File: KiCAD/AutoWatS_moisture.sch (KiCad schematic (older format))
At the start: 20 parts, among them J1 Conn_02x03_Odd_Even, J2 Conn_01x04, U1 ATtiny441-SSU, Y1 YSX321SL

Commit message: Fix Xtal footprint ref
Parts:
- Y1: footprint YSX321SL -> JLCPCB:YSX321SL
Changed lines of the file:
@@
 F 0 "Y1" V 6554 3378 50  0000 L CNN
 F 1 "YSX321SL" V 6645 3378 50  0000 L CNN
-F 2 "YSX321SL" H 7250 3350 50  0001 L CNN
+F 2 "JLCPCB:YSX321SL" H 7250 3350 50  0001 L CNN
 F 3 "https://datasheet.lcsc.com/szlcsc/YSX321SL-30MHZ-10PF-8PPM_C70576.pdf" H 7250 3250 50  0001 L CNN
 F 4 "Crystal" H 7250 3150 50  0001 L CNN "Description"

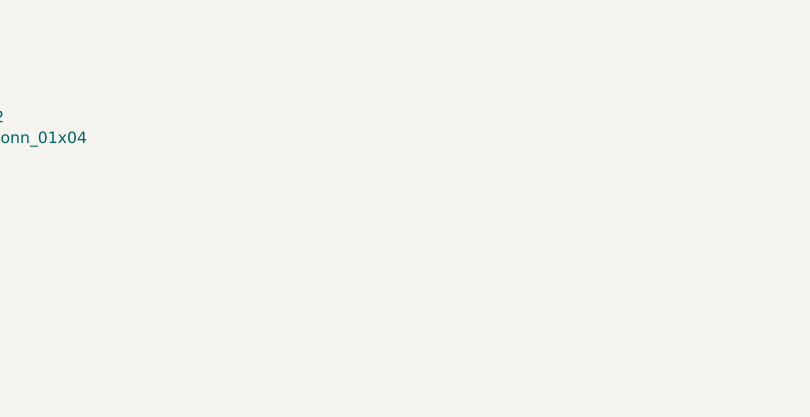
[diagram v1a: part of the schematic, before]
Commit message: Added debug port, silk info and changed the layout a bit
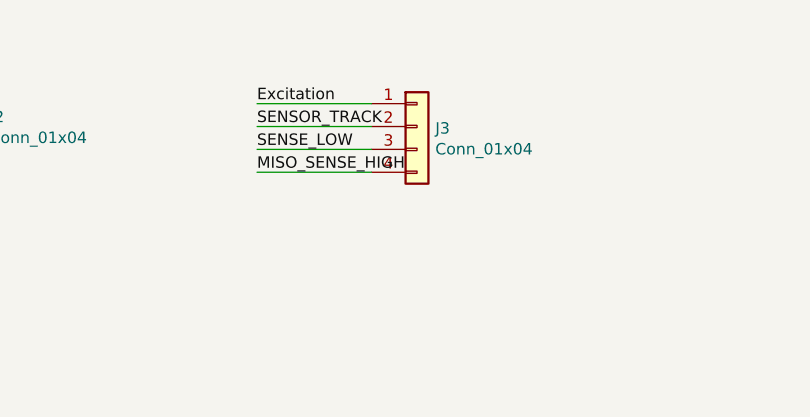
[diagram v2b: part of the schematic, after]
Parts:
- added J3: Conn_01x04, Connector_PinHeader_2.54mm:PinHeader_1x04_P2.54mm_Vertical, symbol Connector_Generic:Conn_01x04
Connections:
- wire segments 66 -> 70
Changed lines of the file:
@@
 	6100 2950 6100 3250
 Connection ~ 6100 3250
+$Comp
+L Connector_Generic:Conn_01x04 J3
+U 1 1 5FB3663B
+P 8400 1300
+F 0 "J3" H 8480 1292 50  0000 L CNN
+F 1 "Conn_01x04" H 8480 1201 50  0000 L CNN
+F 2 "Connector_PinHeader_2.54mm:PinHeader_1x04_P2.54mm_Vertical" H 8400 1300 50  0001 C CNN
+F 3 "~" H 8400 1300 50  0001 C CNN
+	1    8400 1300
+	1    0    0    -1
+$EndComp
+Text Label 7700 1200 0    50   ~ 0
+Excitation
+Text Label 7700 1300 0    50   ~ 0
+SENSOR_TRACK
+Text Label 7700 1500 0    50   ~ 0
+MISO_SENSE_HIGH
+Text Label 7700 1400 0    50   ~ 0
+SENSE_LOW
+Wire Wire Line
+	7700 1200 8200 1200
+Wire Wire Line
+	7700 1300 8200 1300
+Wire Wire Line
+	7700 1400 8200 1400
+Wire Wire Line
+	8200 1500 7700 1500
 $EndSCHEMATC
